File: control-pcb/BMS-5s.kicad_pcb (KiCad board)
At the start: 2 copper layers, 108 x 57.5 mm, 158 parts, among them J2 UEXT, P1 Conn_Switch-N-Sense, P2 CONN_01X06, P3 ON/OFF, P4 USB_Micro-B, P5 CONN_01X02, P6 CONN_01X02, P7 CONN_01X02, Q1 DMN2004K, Q2 BSS84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

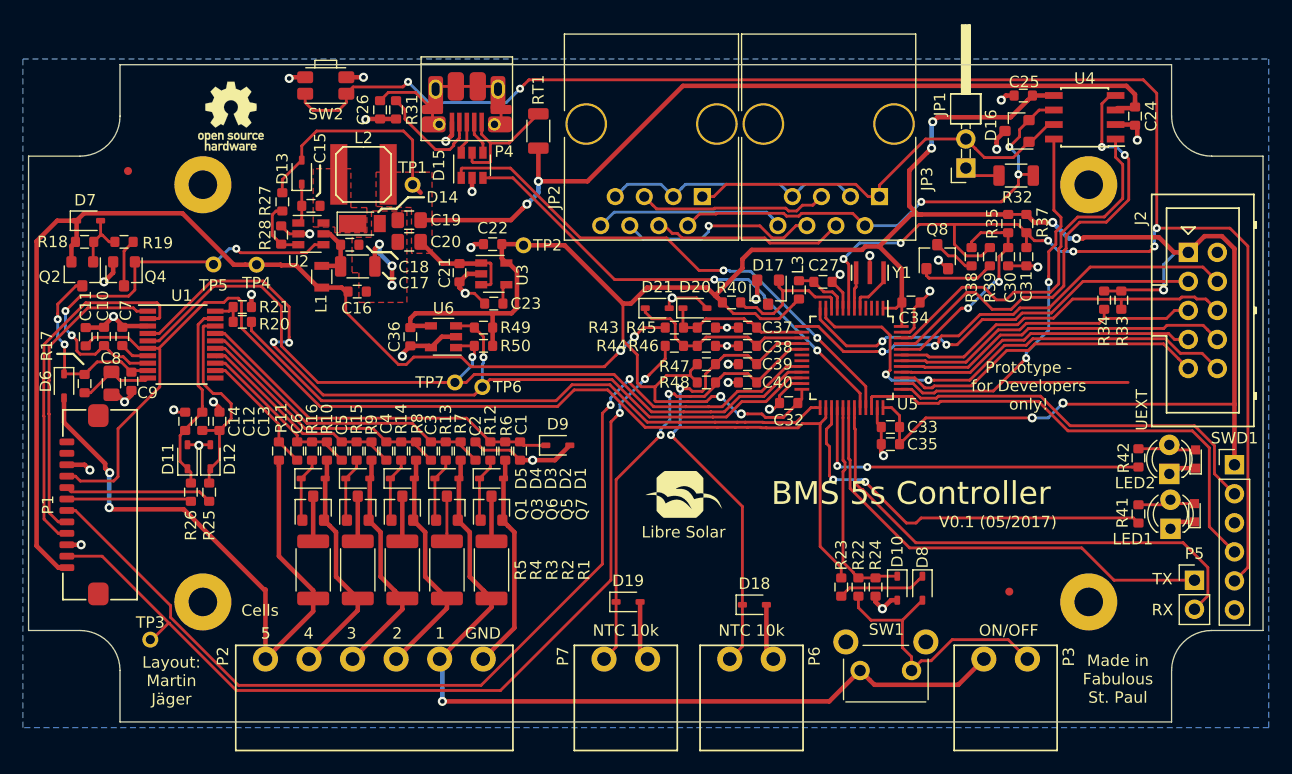
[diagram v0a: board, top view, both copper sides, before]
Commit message: Issues #1, #2 and #4 fixed
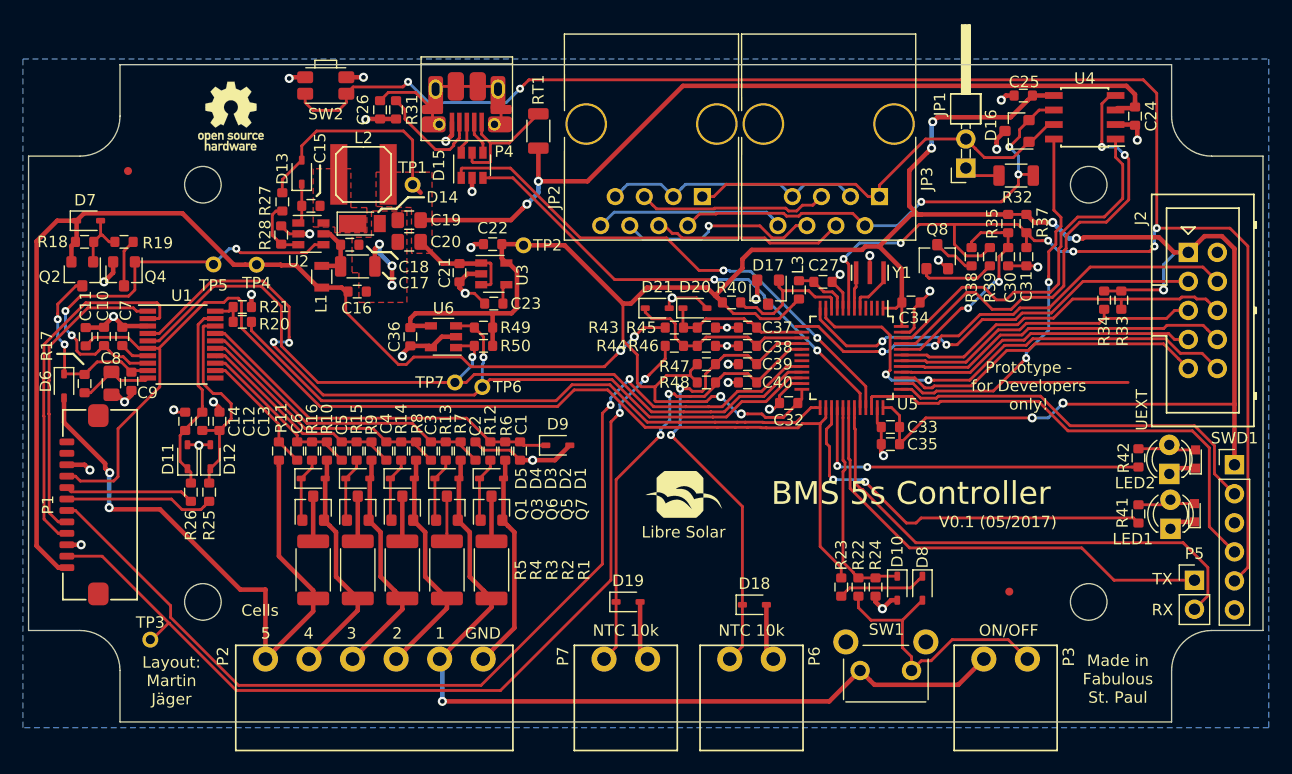
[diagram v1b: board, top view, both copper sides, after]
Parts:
- removed the REF** at (185.2, 107.0)
- removed the REF** at (185.2, 70.5)
- removed the REF** at (107.8, 70.5)
- removed the REF** at (107.8, 107.0)
- added REF**: MountingHole_3.2mm_M3, Mounting_Holes:MountingHole_3.2mm_M3, F.Cu at (185.2, 70.5)
- added REF**: MountingHole_3.2mm_M3, Mounting_Holes:MountingHole_3.2mm_M3, F.Cu at (185.2, 107.0)
- added REF**: MountingHole_3.2mm_M3, Mounting_Holes:MountingHole_3.2mm_M3, F.Cu at (107.8, 107.0)
- added REF**: MountingHole_3.2mm_M3, Mounting_Holes:MountingHole_3.2mm_M3, F.Cu at (107.8, 70.5)
- Q4, Q8: value 2N7002 -> BSS138
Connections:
- P1 pad 7: /BQ76920/R_SENSE- -> /BQ76920/R_SENSE+
- P1 pad 8: /BQ76920/R_SENSE+ -> /BQ76920/R_SENSE-
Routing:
- net /BQ76920/R_SENSE-: track 10.9 -> 11.6 mm

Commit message: Update to KiCAD 5 and minor changes in part selection
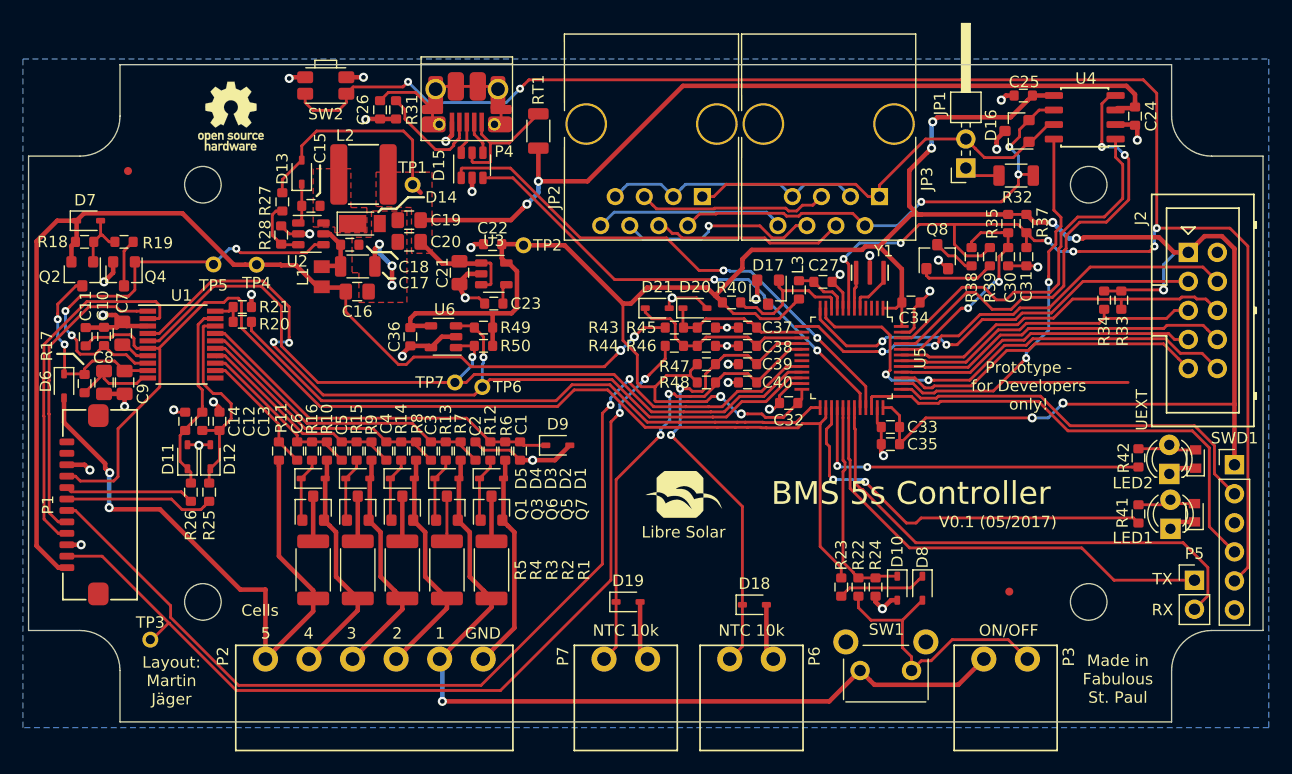
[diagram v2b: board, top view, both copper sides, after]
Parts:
- C16, C21, C7, C9: footprint LibreSolar:C_0603_1608 -> LibreSolar:C_0805_2012
- D14: footprint Diodes_SMD:D_PowerDI-123 -> Diode_SMD:D_PowerDI-123
- D15, U2: footprint TO_SOT_Packages_SMD:SOT-23-6 -> LibreSolar:SOT-23-6
- JP1: footprint Pin_Headers:Pin_Header_Angled_2x01_Pitch2.54mm -> Connector_PinHeader_2.54mm:PinHeader_2x01_P2.54mm_Horizontal
- L1: footprint Inductors_SMD:L_0805 -> Inductor_SMD:L_0805_2012Metric
- LED1, LED2: footprint LEDs:LED_D3.0mm -> LED_THT:LED_D3.0mm
- LED3, LED4: footprint LEDs:LED_0603 -> LED_SMD:LED_0603_1608Metric
- LOGO1: value OPEN_HARDWARE_1 -> OPEN_HARDWARE; footprint Symbols:OSHW-Logo_5.7x6mm_SilkScreen -> Symbol:OSHW-Logo_5.7x6mm_SilkScreen
- P5: footprint Pin_Headers:Pin_Header_Straight_1x02_Pitch2.54mm -> Connector_PinHeader_2.54mm:PinHeader_1x02_P2.54mm_Vertical
- REF** (x4): footprint Mounting_Holes:MountingHole_3.2mm_M3 -> MountingHole:MountingHole_3.2mm_M3
- SWD1: footprint Pin_Headers:Pin_Header_Straight_1x06_Pitch2.54mm -> Connector_PinHeader_2.54mm:PinHeader_1x06_P2.54mm_Vertical
- U1: footprint Housings_SSOP:TSSOP-20_4.4x6.5mm_Pitch0.65mm -> Package_SO:TSSOP-20_4.4x6.5mm_P0.65mm
- U3, U6: footprint TO_SOT_Packages_SMD:SOT-23-5 -> LibreSolar:SOT-23-5
- U4: footprint Housings_SOIC:SOIC-8_3.9x4.9mm_Pitch1.27mm -> LibreSolar:SOIC-8_3.9x4.9mm_Pitch1.27mm
- U5: footprint Housings_QFP:LQFP-48_7x7mm_Pitch0.5mm -> Package_QFP:LQFP-48_7x7mm_P0.5mm
- Y1: footprint LibreSolar:Resonator_Murata_CSTCE -> LibreSolar:Resonator_Murata_CSTCE_G
- moved C8 0.65 mm to (99.1, 87.8)
- moved C9 0.61 mm to (100.9, 87.8)
- moved C7 0.28 mm to (100.7, 83.5)
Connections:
- Y1 pad 2: /MCU/OSC_OUT -> GND
- Y1 pad 3: GND -> /MCU/OSC_OUT
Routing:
- net GND: track 119.0 -> 120.7 mm
- net Net-(C8-Pad1): track 6.69 -> 7.46 mm
- net /TS1: track 107.7 -> 108.2 mm

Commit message: Direct link to schematic added.
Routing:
- net (no net): track 10.4 -> 0.00 mm
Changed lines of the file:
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@@
     (thickness 1.6)
     (drawings 53)
-    (tracks 1476)
+    (tracks 1475)
     (zones 0)
     (modules 158)
@@
   (gr_line (start 200.5 109.5) (end 200.5 68) (layer Edge.Cuts) (width 0.1))
   (gr_line (start 100.5 117.5) (end 192.5 117.5) (layer Edge.Cuts) (width 0.1))
-  (segment (start 188.7 87.8) (end 178.291661 87.8) (width 0.25) (layer F.Cu) (net 0))
   (segment (start 139.399994 75.8) (end 139.4 75.800006) (width 0.4) (layer B.Cu) (net 0))
   (segment (start 141.4 70.2) (end 149.75001 61.84999) (width 0.4) (layer F.Cu) (net 1))

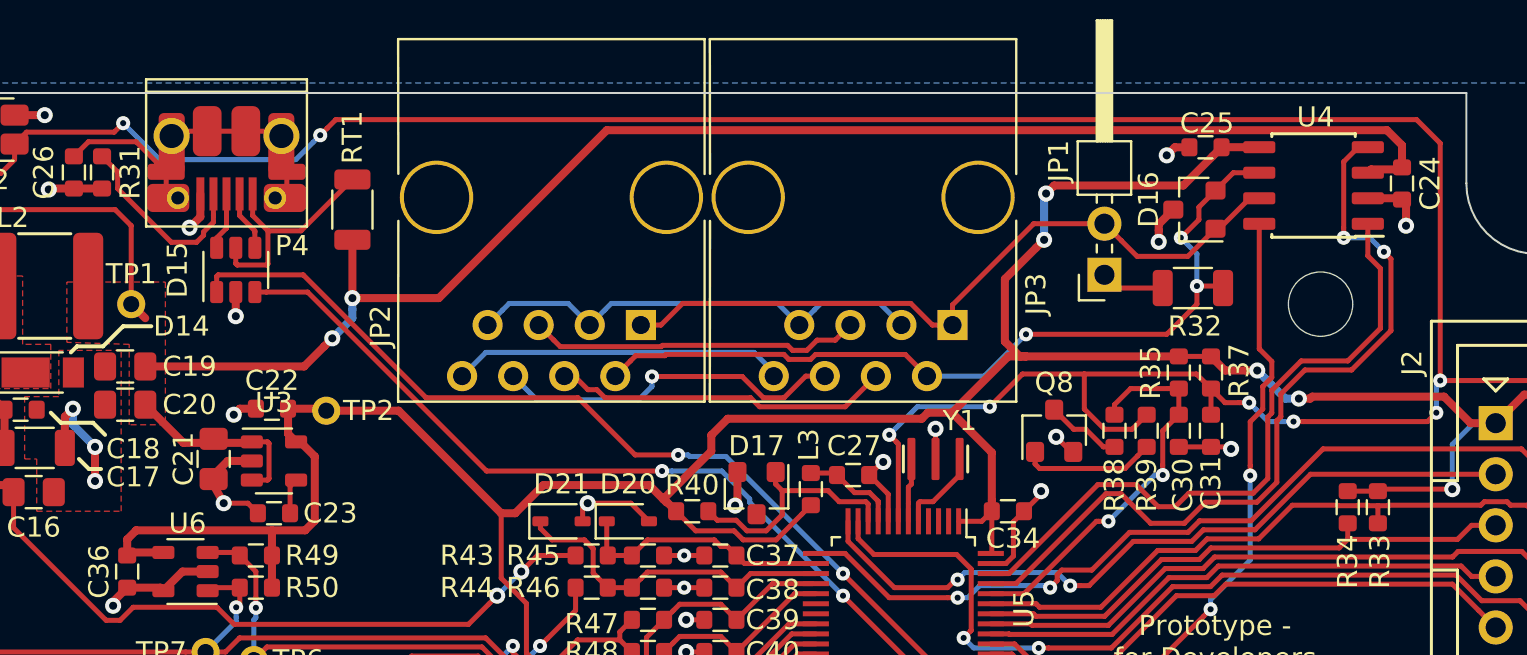
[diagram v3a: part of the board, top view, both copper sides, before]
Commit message: DRC errors corrected
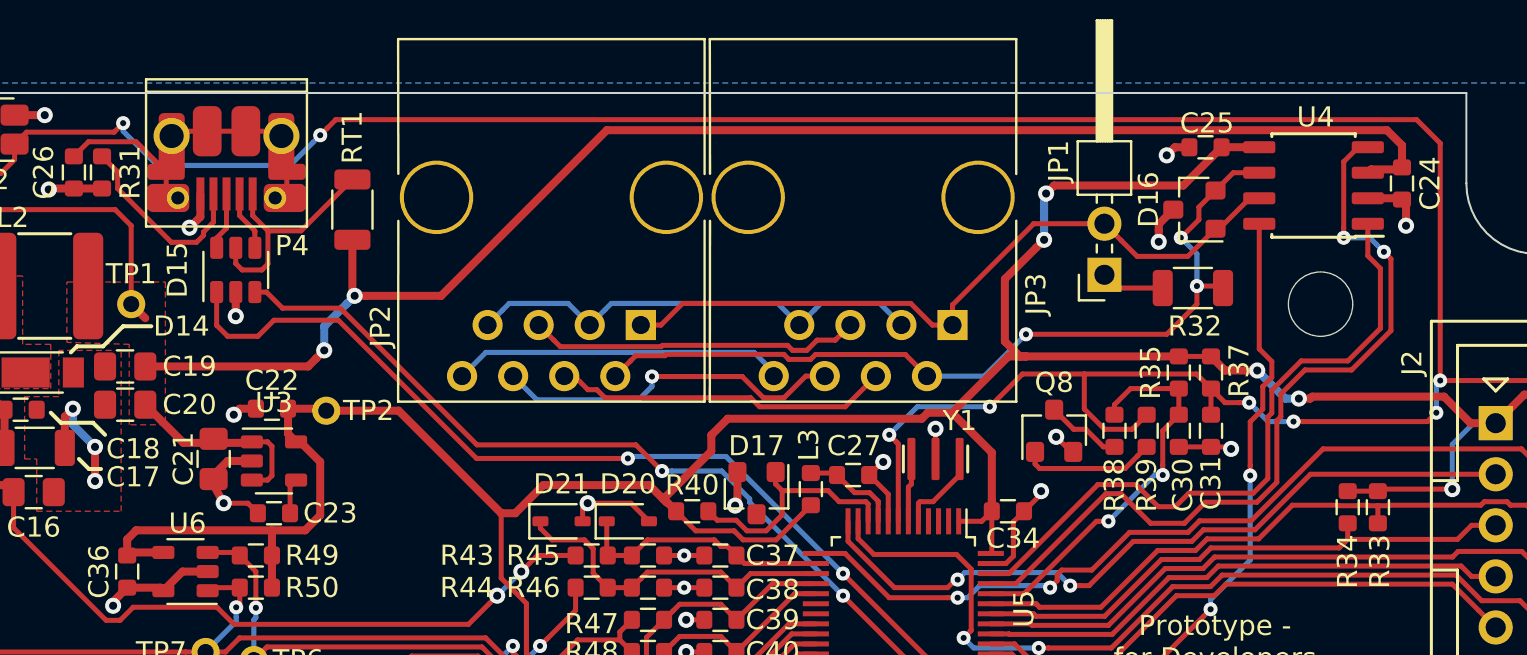
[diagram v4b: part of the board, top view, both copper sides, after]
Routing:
- net /Communication/USB_DP: track 46.0 -> 46.5 mm

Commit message: Diode part number corrected, closing issue #9
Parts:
- D13, D6, D8: value 1N4148W-7-F -> 1N4148WS-7-F
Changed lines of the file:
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@@
       (effects (font (size 1 1) (thickness 0.15)))
     )
-    (fp_text value 1N4148W-7-F (at 0.1 1.9 90) (layer F.Fab)
+    (fp_text value 1N4148WS-7-F (at 0.1 1.9 90) (layer F.Fab)
       (effects (font (size 1 1) (thickness 0.15)))
     )
@@
       (effects (font (size 1 1) (thickness 0.15)))
     )
-    (fp_text value 1N4148W-7-F (at 0.1 1.9 270) (layer F.Fab)
+    (fp_text value 1N4148WS-7-F (at 0.1 1.9 270) (layer F.Fab)
       (effects (font (size 1 1) (thickness 0.15)))
     )
@@
       (effects (font (size 1 1) (thickness 0.15)))
     )
-    (fp_text value 1N4148W-7-F (at 0.1 1.9 270) (layer F.Fab)
-      (effects (font (size 1 1) (thickness 0.15)))
-    )
+    (fp_text value 1N4148WS-7-F (at 0.1 1.9 270) (layer F.Fab)
+      (effects (font (size 1 1) (thickness 0.15)))
+    )
